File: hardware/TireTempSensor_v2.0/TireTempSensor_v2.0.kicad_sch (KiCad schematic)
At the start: 6 parts

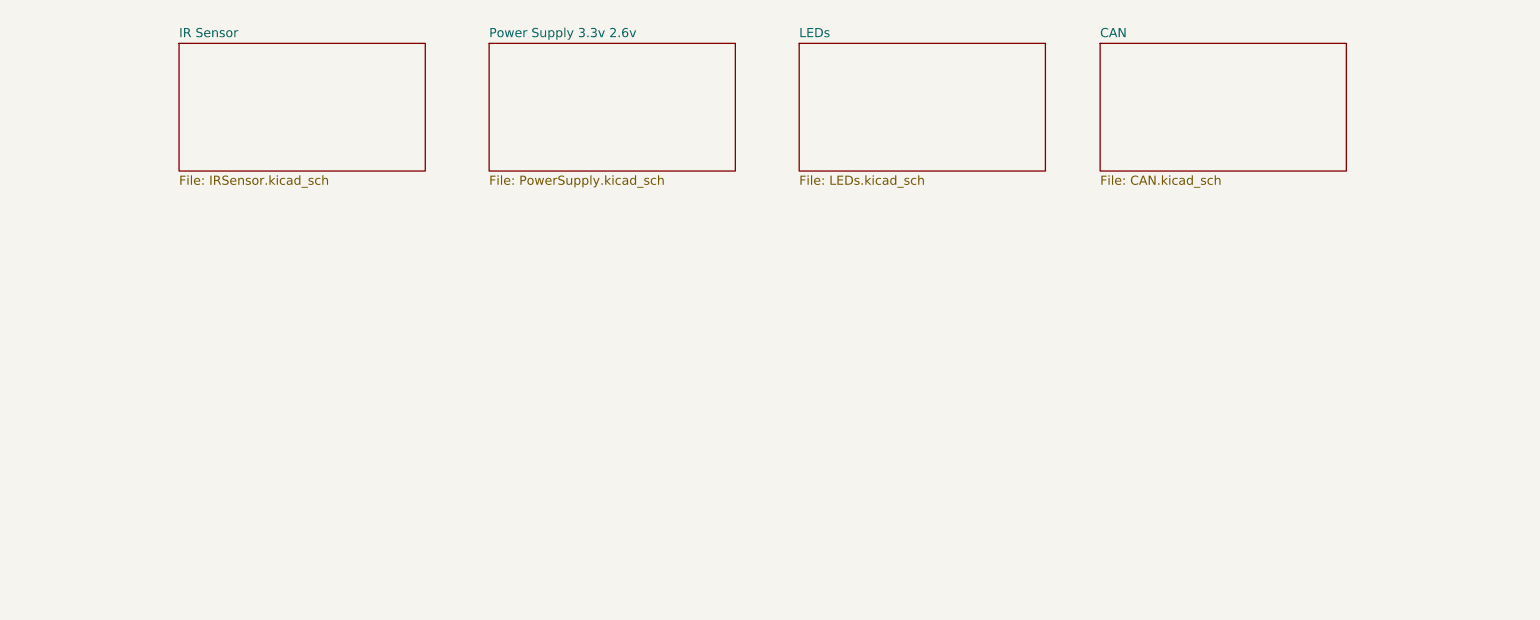
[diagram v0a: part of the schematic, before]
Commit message: PFET & buck caps models
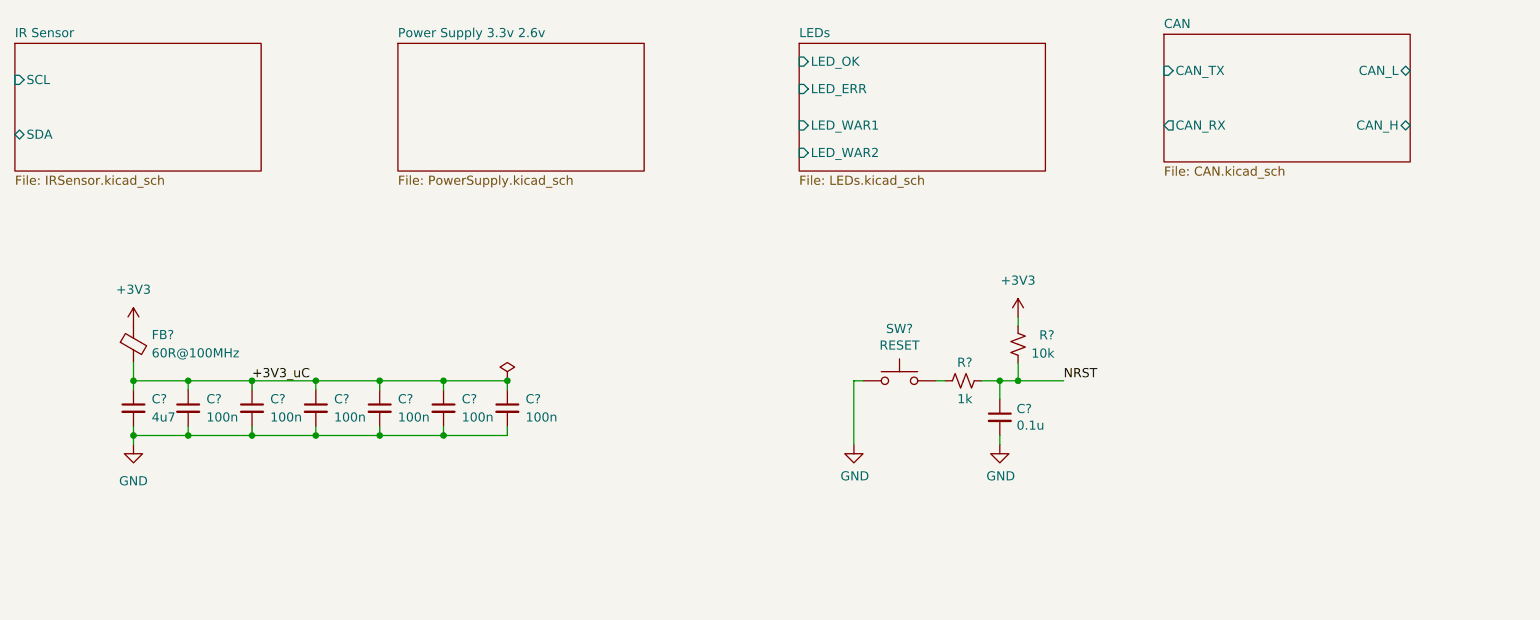
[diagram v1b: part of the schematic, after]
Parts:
- added C? (x6): 100n, Capacitor_SMD:C_0603_1608Metric, symbol Device:C_Small
- added C?: 0.1u, Capacitor_SMD:C_0603_1608Metric, symbol SB-Spoko-Bezpieczniki-rescue:C_Small-Device
- added C?: 4u7, Capacitor_SMD:C_0603_1608Metric, symbol Device:C_Small
- added FB?: 60R@100MHz, Inductor_SMD:L_0603_1608Metric, symbol Device:FerriteBead_Small
- added R?: 10k, Resistor_SMD:R_0603_1608Metric, symbol Device:R_Small_US
- added R?: 1k, Resistor_SMD:R_0603_1608Metric, symbol Device:R_Small_US
- added SW?: RESET, BUTTON:434781025816, symbol SB-Spoko-Bezpieczniki-rescue:SW_Push-Switch
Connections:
- net +3V3: now also FB?.1, R?.2
- net GND: now also C?.2, C?.2, C?.2, C?.2, C?.2, C?.2, C?.2, C?.2, SW?.1
- net NRST: now also C?.1, R?.1, R?.2
- new net: R?.1, SW?.2
- new net +3V3_uC: C?.1, C?.1, C?.1, C?.1, C?.1, C?.1, C?.1, FB?.2
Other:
- sheet CAN ports: added CAN_H, CAN_L, CAN_RX, CAN_TX; removed none
- sheet IR Sensor ports: added SCL, SDA; removed none
- sheet LEDs ports: added LED_ERR, LED_OK, LED_WAR1, LED_WAR2; removed none

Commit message: schematic complete
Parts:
- removed C? (x2): 8p, Capacitor_SMD:C_0603_1608Metric, symbol Device:C_Small
- removed C?: 0.1u, Capacitor_SMD:C_0603_1608Metric, symbol SB-Spoko-Bezpieczniki-rescue:C_Small-Device
- removed R?: 47, Resistor_SMD:R_0603_1608Metric, symbol Device:R_Small_US
- removed R?: 10k, Resistor_SMD:R_0603_1608Metric, symbol Device:R_Small_US
- removed R?: 1k, Resistor_SMD:R_0603_1608Metric, symbol Device:R_Small_US
- removed SW?: RESET, BUTTON:434781025816, symbol SB-Spoko-Bezpieczniki-rescue:SW_Push-Switch
- removed Y?: 16MGHz, Crystal:Crystal_SMD_SeikoEpson_TSX3225-4Pin_3.2x2.5mm, symbol Device:Crystal_GND24_Small
- added C? (x2): 8p, Capacitor_SMD:C_0603_1608Metric, symbol Device:C_Small
- added C?: 0.1u, Capacitor_SMD:C_0603_1608Metric, symbol SB-Spoko-Bezpieczniki-rescue:C_Small-Device
- added R?: 100k, Resistor_SMD:R_0603_1608Metric, symbol Device:R_Small_US
- added R?: 10k, Resistor_SMD:R_0603_1608Metric, symbol Device:R_Small_US
- added R?: 47, Resistor_SMD:R_0603_1608Metric, symbol Device:R_Small_US
- added R?: 1k, Resistor_SMD:R_0603_1608Metric, symbol Device:R_Small_US
- added SW?: RESET, BUTTON:434781025816, symbol SB-Spoko-Bezpieczniki-rescue:SW_Push-Switch
- added U?: STM32L476JEYx, Package_CSP:ST_WLCSP-72_Die415, symbol MCU_ST_STM32L4:STM32L476JEYx
- added Y?: 16MGHz, Crystal:Crystal_SMD_SeikoEpson_TSX3225-4Pin_3.2x2.5mm, symbol Device:Crystal_GND24_Small
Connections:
- net +3V3: now also R?.2
- net +3V3_uC: now also U?.A1 (VDDUSB), U?.A9 (VDD), U?.B6 (VDDIO2), U?.B9 (VBAT), U?.H9 (VDDA), U?.J1 (VDD), U?.J8 (VDD)
- net GND: now also C?.2, C?.2, C?.2, R?.2, SW?.1, U?.A8 (VSS), U?.B1 (VSS), U?.G9 (VSSA), U?.J2 (VSS), U?.J9 (VSS), Y?.2, Y?.4
- net NRST: now also C?.1, R?.1, R?.2, U?.E9 (NRST)
- net OSC_IN: now also C?.1, U?.D9 (PH0), Y?.1
- net OSC_OUT: now also R?.1, U?.D8 (PH1)
- net SWCLK: now also U?.B2 (PA14)
- net SWDIO: now also U?.C2 (PA13)
- net SWO: now also U?.A6 (PB3)
- new net: R?.1, U?.D7 (BOOT0)
- new net: R?.1, SW?.2
- new net: C?.1, R?.2, Y?.3
- new net CAN RX: U?.D1 (PA11)
- new net CAN TX: U?.C1 (PA12)
- new net LED ERR: U?.J6 (PC5)
- new net LED OK: U?.H7 (PA3)
- new net LED WAR1: U?.J4 (PB1)
- new net LED WAR2: U?.H5 (PA6)
- new net SCL: U?.H2 (PB13)
- new net SDA: U?.G2 (PB14)
- no-connect marks 0 -> 45
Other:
- note added: "CAN"
- note added: "CONNECTORS"
- note added: "LEDS"
- note added: "NRST"
- note added: "OSC"
- note added: "POWER FILTRATION"
- note added: "POWER SUPPLY"
- note added: "STM32L476JEY6TR"
- note added: "TEMPERATURE SENSOR"
- title: (none) -> Tire Temp Sensor v2.0
- moved on the sheet: C?, FB?, J?

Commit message: erc tests passed
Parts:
- removed C?: 0.1u, Capacitor_SMD:C_0603_1608Metric, symbol SB-Spoko-Bezpieczniki-rescue:C_Small-Device
- removed R?: 10k, Resistor_SMD:R_0603_1608Metric, symbol Device:R_Small_US
- removed R?: 1k, Resistor_SMD:R_0603_1608Metric, symbol Device:R_Small_US
- removed SW?: RESET, BUTTON:434781025816, symbol SB-Spoko-Bezpieczniki-rescue:SW_Push-Switch
- added 10k1, R3: 1k, symbol Device:R_Small_US
- added C11: 0.1u, symbol Device:C_Small
- added C8: 100n, Capacitor_SMD:C_0603_1608Metric, symbol Device:C_Small
- added SW1: RESET, symbol Switch:SW_MEC_5G
- gave numbers to parts that had none: 16
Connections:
- net +3V3: now also 10k1.2
- net +3V3_uC: now also C8.1
- net GND: now also C11.2, C8.2, SW1.1 (A), SW1.2 (A)
- net NRST: now also 10k1.1, C11.1, R3.2
- new net: R3.1, SW1.3 (B), SW1.4 (B)
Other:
- moved on the sheet: C1, C10, C2, C3, C4, C5, C6, C7, C9, FB1, J1, J2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

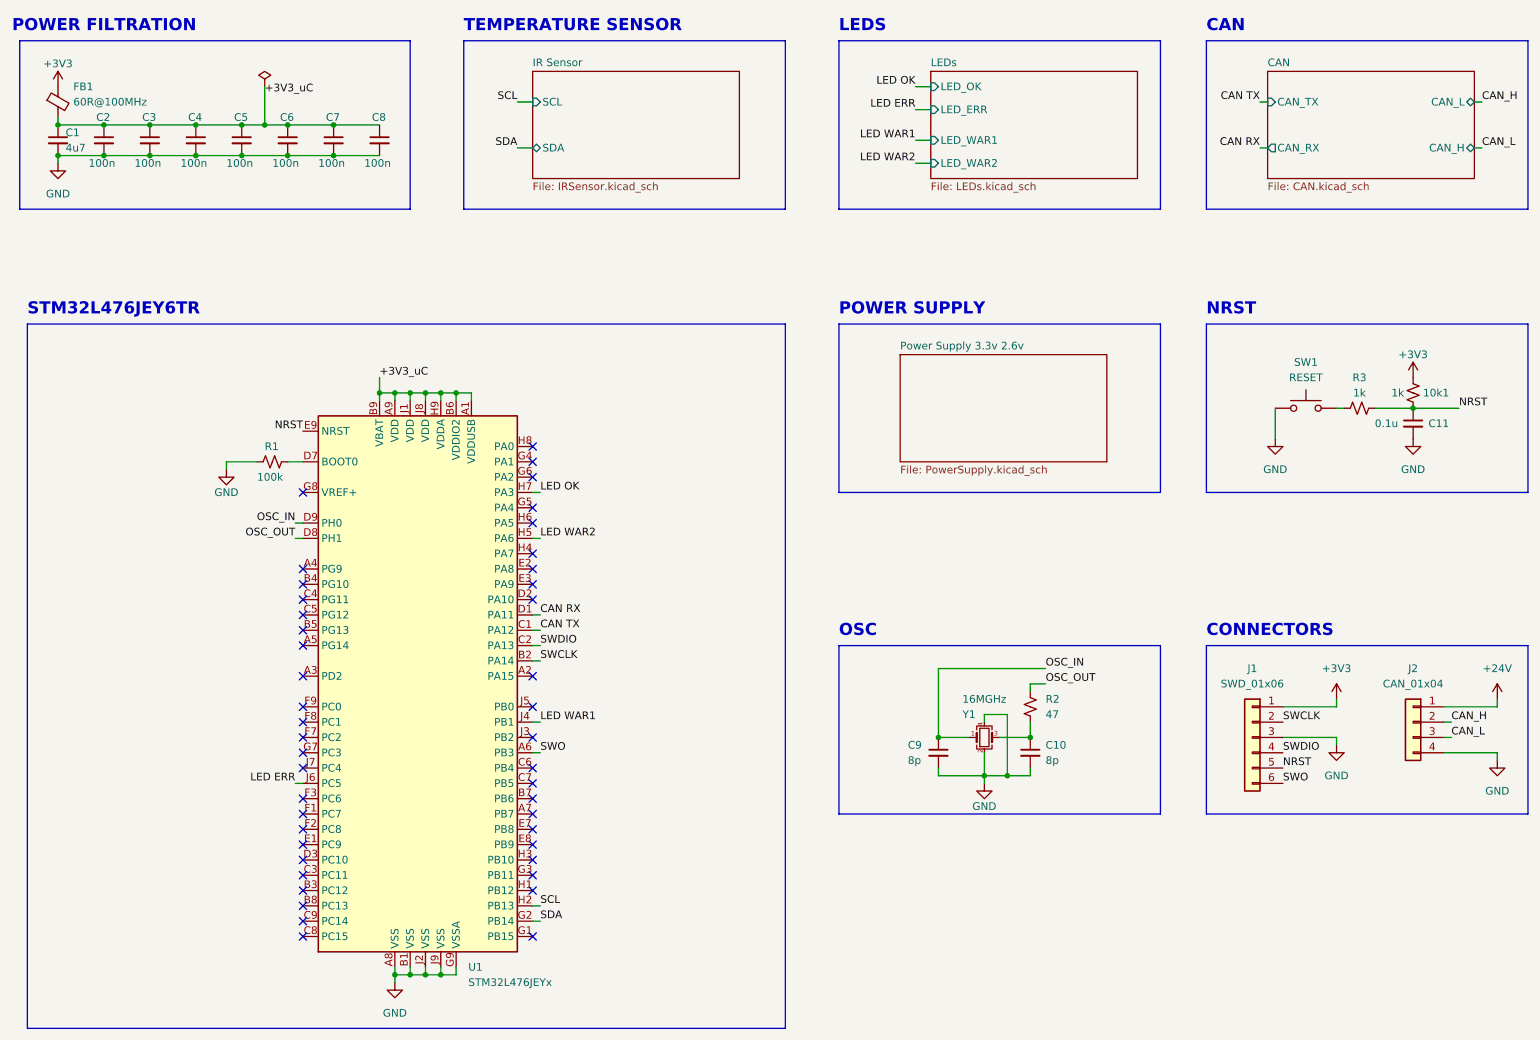
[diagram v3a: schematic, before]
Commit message: changed the stm
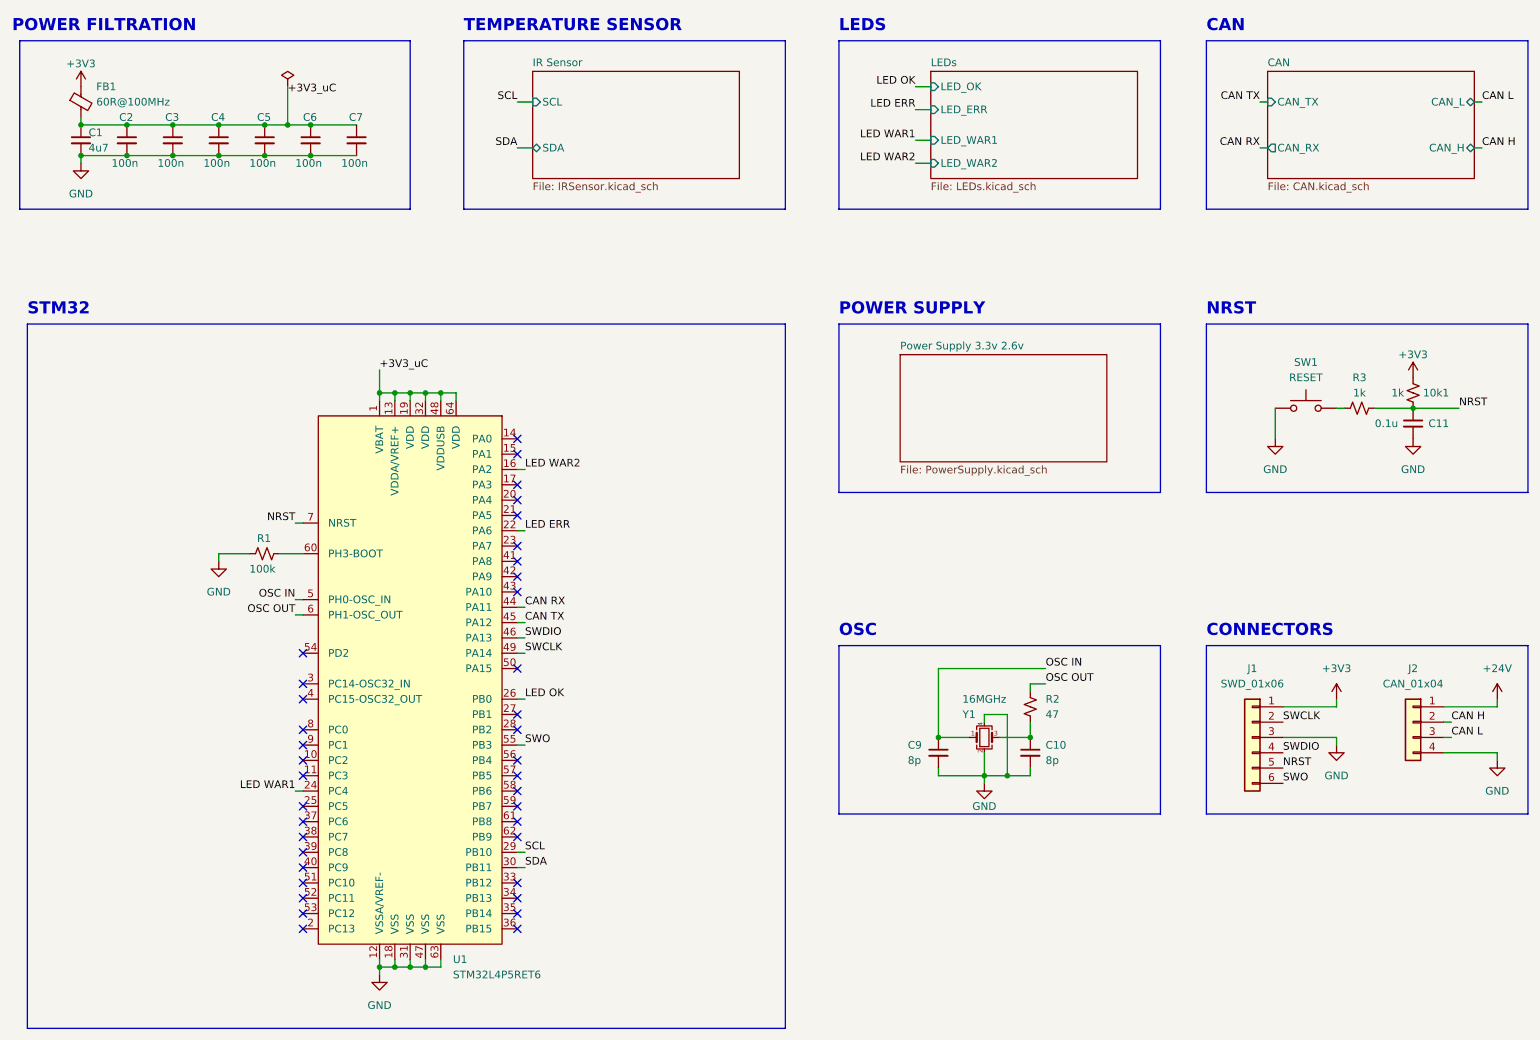
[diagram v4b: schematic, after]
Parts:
- removed C8: 100n, Capacitor_SMD:C_0603_1608Metric, symbol Device:C_Small
- removed U1: STM32L476JEYx, Package_CSP:ST_WLCSP-72_Die415, symbol MCU_ST_STM32L4:STM32L476JEYx
- added U1: STM32L4P5RET6, Package_QFP:LQFP-64_10x10mm_P0.5mm, symbol stm32:STM32L4P5RET6
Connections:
- net +3V3_uC: now also U1.1 (VBAT), U1.13 (VDDA/VREF+), U1.19 (VDD), U1.32 (VDD), U1.48 (VDDUSB), U1.64 (VDD)
- net CAN RX: now also U1.44 (PA11)
- net CAN TX: now also U1.45 (PA12)
- net GND: now also U1.12 (VSSA/VREF-), U1.18 (VSS), U1.31 (VSS), U1.47 (VSS), U1.63 (VSS)
- net LED ERR: now also U1.22 (PA6)
- net LED OK: now also U1.26 (PB0)
- net LED WAR1: now also U1.24 (PC4)
- net LED WAR2: now also U1.16 (PA2)
- net NRST: now also U1.7 (NRST)
- net SCL: now also U1.29 (PB10)
- net SDA: now also U1.30 (PB11)
- net SWCLK: now also U1.49 (PA14)
- net SWDIO: now also U1.46 (PA13)
- net SWO: now also U1.55 (PB3)
- net at R1.1: now also U1.60 (PH3-BOOT)
- net CAN_H renamed CAN H
- net CAN_L renamed CAN L
- net OSC_IN renamed OSC IN
- net OSC IN: now also U1.5 (PH0-OSC_IN)
- net OSC_OUT renamed OSC OUT
- net OSC OUT: now also U1.6 (PH1-OSC_OUT)
- no-connect marks 45 -> 38
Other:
- note added: "STM32"
- note removed: "STM32L476JEY6TR"
- moved on the sheet: C1, C2, C3, C4, C5, C6, C7, FB1
